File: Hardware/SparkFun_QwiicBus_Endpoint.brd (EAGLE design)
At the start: 44.5 x 25.4 mm, 61 parts, among them J1 QWIIC, J2 QWIIC, J3 RJ45, U1 PCA9615

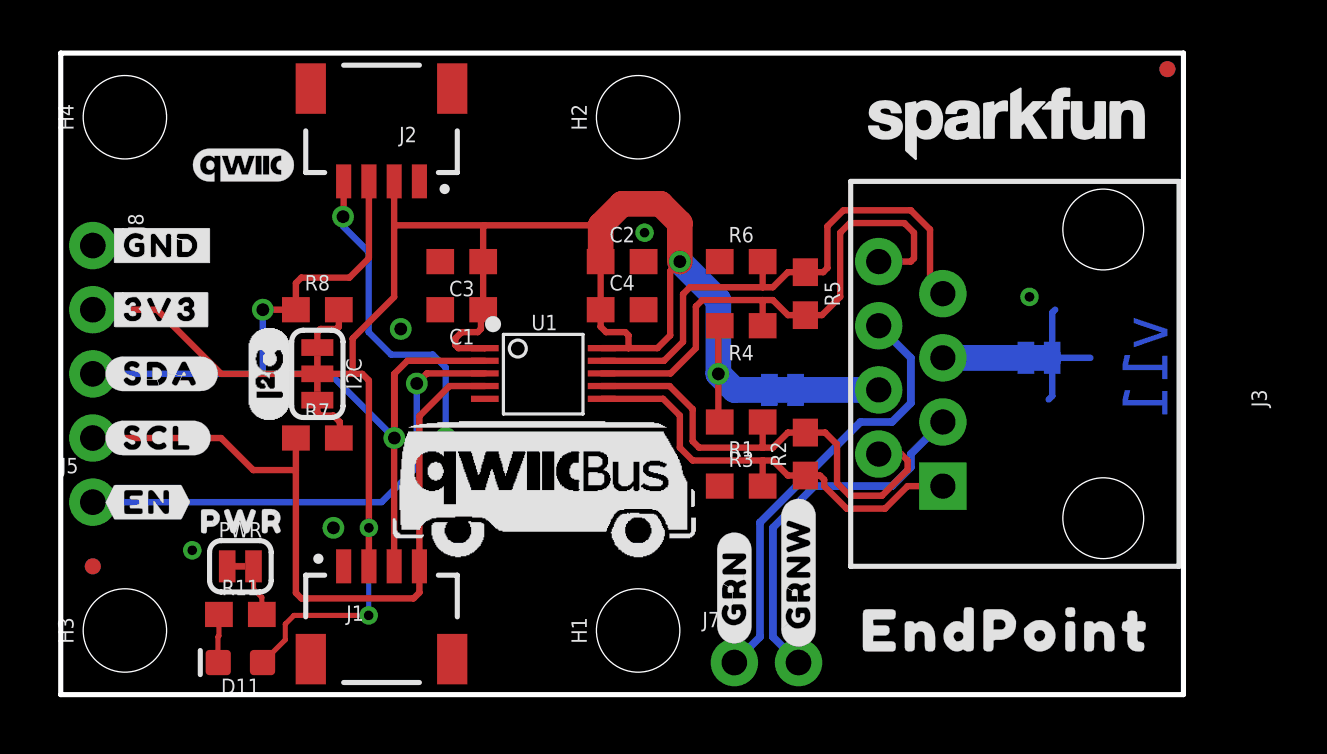
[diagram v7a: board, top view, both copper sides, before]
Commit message: removing blue pair access
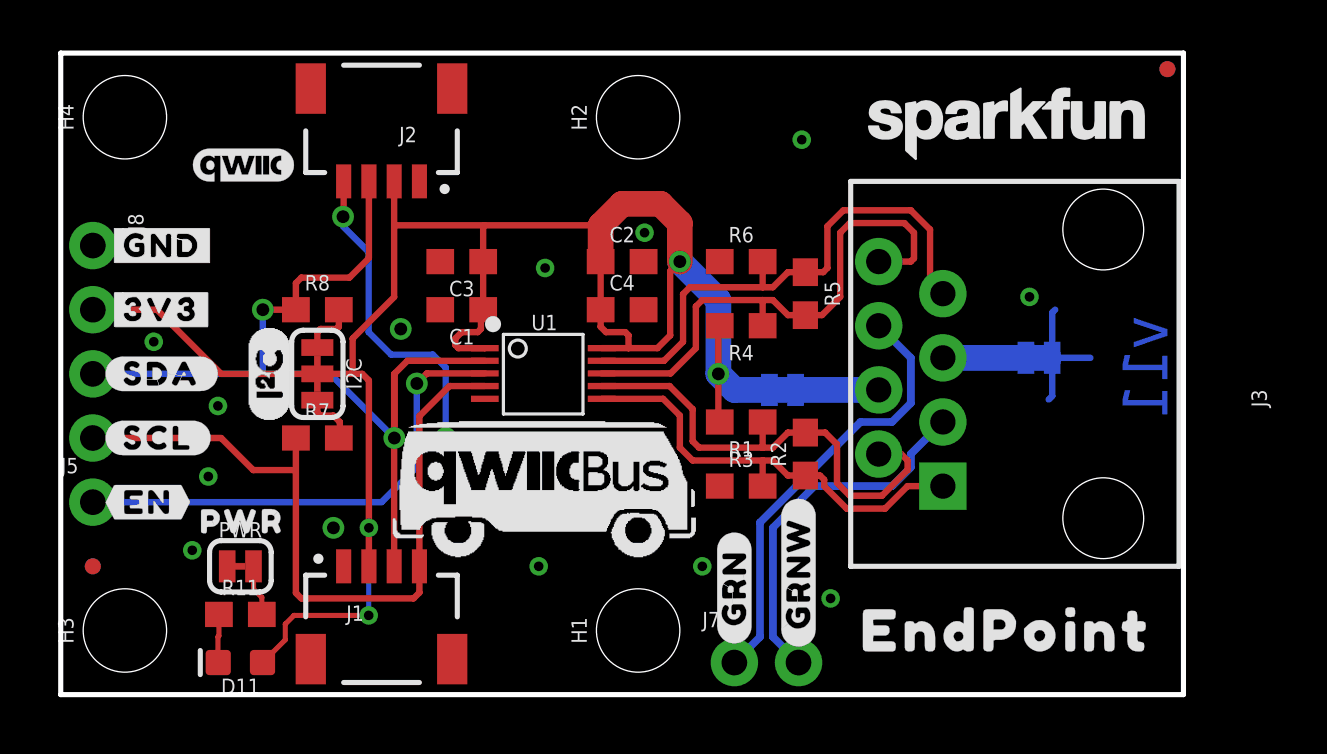
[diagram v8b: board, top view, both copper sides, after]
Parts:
- removed U$14: (no value), output:#VDDB#0
- removed U$2: (no value), output:#HV##0
- added U$12: (no value), output:#VDDA#0
- added U$13: (no value), output:#HV##1
- renumbered VDDB to VDDA
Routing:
- net GND: vias 5 -> 13
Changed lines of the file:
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@@
 </element>
 <element name="LOGO1" library="SparkFun-Aesthetics" package="OSHW-LOGO-M" value="OSHW-LOGOM" x="12.7" y="2.54" smashed="yes" rot="MR0"/>
-<element name="VDDB" library="SparkFun-Jumpers" package="SMT-JUMPER_2_NC_TRACE_SILK" package3d_urn="urn:adsk.eagle:package:39281/1" value="JUMPER-SMT_2_NC_TRACE_SILK" x="28.575" y="12.065" smashed="yes" rot="MR180">
+<element name="VDDA" library="SparkFun-Jumpers" package="SMT-JUMPER_2_NC_TRACE_SILK" package3d_urn="urn:adsk.eagle:package:39281/1" value="JUMPER-SMT_2_NC_TRACE_SILK" x="28.575" y="12.065" smashed="yes" rot="MR180">
 <attribute name="NAME" x="28.575" y="10.922" size="0.6096" layer="26" font="vector" ratio="20" rot="MR180" align="bottom-center"/>
 <attribute name="VALUE" x="28.575" y="13.208" size="0.6096" layer="28" font="vector" ratio="20" rot="MR180" align="top-center"/>
@@
 <element name="U$10" library="output" package="#SCL#0" value="" x="1.778" y="10.16" smashed="yes"/>
 <element name="U$11" library="output" package="#EN#0" value="" x="1.778" y="7.62" smashed="yes"/>
-<element name="U$14" library="output" package="#VDDB#0" value="" x="28.575" y="18.288" smashed="yes" rot="MR270"/>
 <element name="U$15" library="output" package="#SDA#0" value="" x="6.223" y="12.7" smashed="yes" rot="MR0"/>
 <element name="U$16" library="output" package="#SCL#0" value="" x="5.969" y="10.16" smashed="yes" rot="MR0"/>
@@
 <element name="U$28" library="QwiicBus#working#Logo#jpg (2)" package="QWIICBUS#WORKING#LOGO#JPG" value="" x="19.558" y="8.509" smashed="yes"/>
 <element name="U$23" library="QwiicBus#working#Logo#jpg (2)" package="QWIICBUS#WORKING#LOGO#JPG" value="" x="18.442" y="13.874" smashed="yes" rot="MR0"/>
-<element name="U$2" library="output" package="#HV##0" value="" x="29.21" y="1.778" smashed="yes" rot="MR90"/>
 <element name="U$3" library="output" package="#HV##0" value="" x="26.67" y="1.778" smashed="yes" rot="MR90"/>
+<element name="U$12" library="output" package="#VDDA#0" value="" x="28.575" y="18.542" smashed="yes" rot="MR270"/>
+<element name="U$13" library="output" package="#HV##1" value="" x="29.21" y="1.778" smashed="yes" rot="MR90"/>
 </elements>
 <signals>
@@
 <wire x1="39.2557" y1="13.335" x2="39.2557" y2="11.8237" width="0.254" layer="16"/>
 <wire x1="39.2557" y1="11.8237" x2="39.116" y2="11.684" width="0.254" layer="16"/>
+<via x="5.842" y="8.636" extent="1-16" drill="0.381"/>
+<via x="6.223" y="11.43" extent="1-16" drill="0.381"/>
+<via x="3.683" y="13.97" extent="1-16" drill="0.381"/>
+<via x="18.923" y="5.08" extent="1-16" drill="0.381"/>
+<via x="19.177" y="16.891" extent="1-16" drill="0.381"/>
+<via x="29.337" y="21.971" extent="1-16" drill="0.381"/>
+<via x="25.4" y="5.08" extent="1-16" drill="0.381"/>
+<via x="30.48" y="3.81" extent="1-16" drill="0.381"/>
 </signal>
 <signal name="3.3V">
@@
 <wire x1="21.416" y1="13.7175" x2="22.479" y2="13.7175" width="0.254" layer="1"/>
 <wire x1="22.479" y1="14.224" x2="22.479" y2="13.7175" width="0.254" layer="1"/>
-<contactref element="VDDB" pad="1"/>
+<contactref element="VDDA" pad="1"/>
 <wire x1="21.375" y1="15.24" x2="21.375" y2="14.566" width="0.254" layer="1"/>
 <wire x1="21.375" y1="14.566" x2="21.59" y2="14.351" width="0.254" layer="1"/>
@@
 </signal>
 <signal name="N$1">
-<contactref element="VDDB" pad="2"/>
+<contactref element="VDDA" pad="2"/>
 <contactref element="J3" pad="4"/>
 <wire x1="29.0957" y1="12.065" x2="32.385" y2="12.065" width="1.016" layer="16"/>
